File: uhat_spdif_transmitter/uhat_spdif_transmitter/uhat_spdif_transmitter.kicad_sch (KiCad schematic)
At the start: 75 parts, among them J1 GPIO_CONNECTOR, Q1 SS8050, SW1 SW_Push, U1 PLT131/T8, U10 USBLC6-2SC6, U2 LR8103A-T12, U4 W25Q32JVSSIQ, U5 24LC256T-I/SN, U6 PLT131/T8, U8 ICE40UP5K-SG48I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

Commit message: layout
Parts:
- removed SW1: SW_Push, Button_Switch_SMD:SW_SPST_EVQQ2, symbol Switch:SW_Push
- added J2: Conn_02x03_Odd_Even, Connector_PinHeader_2.54mm:PinHeader_2x03_P2.54mm_Vertical_SMD, symbol Connector_Generic:Conn_02x03_Odd_Even
- added J3: Conn_01x03_Pin, Connector_PinHeader_2.54mm:PinHeader_1x03_P2.54mm_Vertical_SMD_Pin1Left, symbol Connector:Conn_01x03_Pin
- added SW1: SPEH110100, Locrius_KiCad:SW-SMD_L6.0-W6.0-LS6.6, symbol Locrius_KiCad:SPEH110100
- R3, R4: value 27R -> 68R
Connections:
- net QSPI_SCLK is gone; now on net SPI_SCK: U8.15 (IOB_34a_SPI_SCK)
- net QSPI_SD0 is gone; now on net SPI_MOSI: U8.14 (IOB_32a_SPI_SO)
- net QSPI_SD1 is gone; now on net SPI_MISO: U8.17 (IOB_33b_SPI_SI)
- net QSPI_SS is gone; now on net SPI_SS: U8.16 (IOB_35b_SPI_SS)
- net GND: now also J2.5 (Pin_5), J2.6 (Pin_6), J3.3 (Pin_3), SW1.1
- net PCM_BCLK: now also J2.2 (Pin_2); no longer R13.2
- net PCM_DOUT: now also J2.1 (Pin_1); no longer R14.2
- net PCM_FCLK: now also J3.1 (Pin_1); no longer R12.2
- net USER_SW: now also SW1.2
- net DM renamed DN
- net QSPI_SD2: no longer names the net of U8.10 (IOB_18a)
- net QSPI_SD3: no longer names the net of U8.20 (IOB_25b_G3)
- new net FPGA_BCLK: J2.4 (Pin_4), R13.2
- new net FPGA_DOUT: J2.3 (Pin_3), R14.2
- new net FPGA_FCLK: J3.2 (Pin_2), R12.2
- no-connect marks 25 -> 41
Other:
- note added: "APX Header"

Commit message: Finish routing
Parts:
- removed D7: C2290, LED_SMD:LED_0805_2012Metric, symbol Device:LED
- removed LED1: TC5050RGBF08-3CJH-AF53A, Locrius_KiCad:LED-SMD_6P-L5.0-W5.0-TL_TC5050RGBF08, symbol Locrius_KiCad:TC5050RGBF08-3CJH-AF53A
- removed Q1: SS8050, Package_TO_SOT_SMD:SOT-23, symbol Transistor_BJT:SS8050
- removed R26: 2k2, Resistor_SMD:R_0603_1608Metric_Pad0.98x0.95mm_HandSolder, symbol Device:R
- removed SW1: SPEH110100, Locrius_KiCad:SW-SMD_L6.0-W6.0-LS6.6, symbol Locrius_KiCad:SPEH110100
- removed U1, U6: PLT131/T8, Locrius_KiCad:OPTO-TH_PLT131-T8, symbol Locrius_KiCad:PLT131_T8
- added J4: Conn_02x03_Odd_Even, Connector_PinHeader_2.54mm:PinHeader_2x03_P2.54mm_Vertical, symbol Connector_Generic:Conn_02x03_Odd_Even
- added LED2: MHS110RGBCT, Locrius_KiCad:LED-ARRAY-SMD_MHS110RGBCT, symbol Locrius_KiCad:MHS110RGBCT
- added SW2: SKRTLAE010, Locrius_KiCad:KEY-SMD_SKRTLAE010, symbol Locrius_KiCad:SKRTLAE010
- added U1, U6: PLR237/T10BK, Locrius_KiCad:OPTO-TH_PLR237-T10BK, symbol Locrius_KiCad:PLR237_T10BK
- J2: footprint Connector_PinHeader_2.54mm:PinHeader_2x03_P2.54mm_Vertical_SMD -> Connector_PinHeader_2.54mm:PinHeader_2x03_P2.54mm_Vertical
- J3: footprint Connector_PinHeader_2.54mm:PinHeader_1x03_P2.54mm_Vertical_SMD_Pin1Left -> Connector_PinHeader_2.54mm:PinHeader_1x03_P2.54mm_Vertical
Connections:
- net +3V3: now also LED2.2 (+)
- net GND: now also J4.1 (Pin_1), J4.3 (Pin_3), J4.5 (Pin_5), SW2.1, SW2.3, SW2.4, SW2.5, U1.2 (GND), U6.2 (GND)
- net OPT1: now also U1.3 (VOUT)
- net OPT2: now also U6.3 (VOUT)
- net USER_SW: now also SW2.2
- net at C13.1, FB2.2: now also U6.1 (VCC)
- net at R18.2: now also LED2.1 (-)
- net at C12.1, FB1.2: now also U1.1 (VCC)
- net at R19.2: now also LED2.3 (-)
- net at R20.2: now also LED2.4 (-)
- net at U8.10 (IOB_18a): now also J4.4 (Pin_4)
- net at U8.11 (IOB_20a): now also J4.6 (Pin_6)
- net at U8.9 (IOB_16a): now also J4.2 (Pin_2)
- net USER_LED: no longer names the net of U8.19 (IOB_29b)
- no-connect marks 41 -> 43
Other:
- moved on the sheet: R18, R19, R20

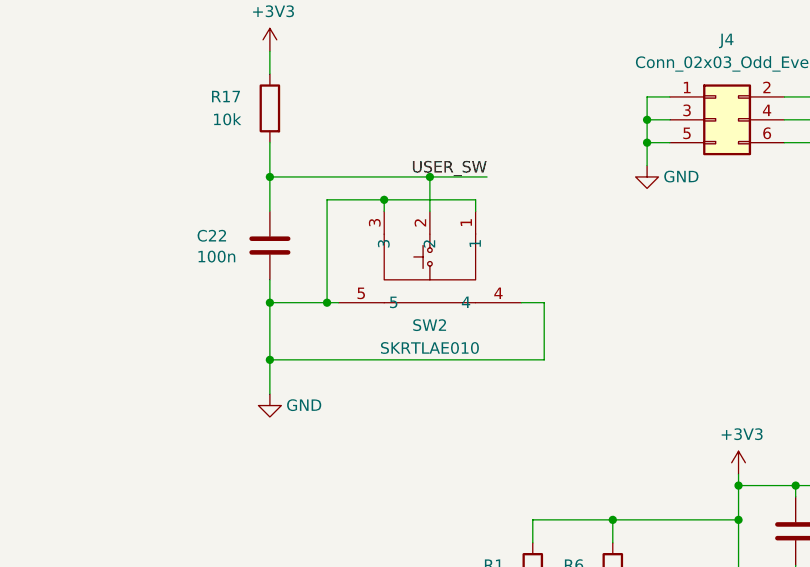
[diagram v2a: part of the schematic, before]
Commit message: Change push button, add barcode location
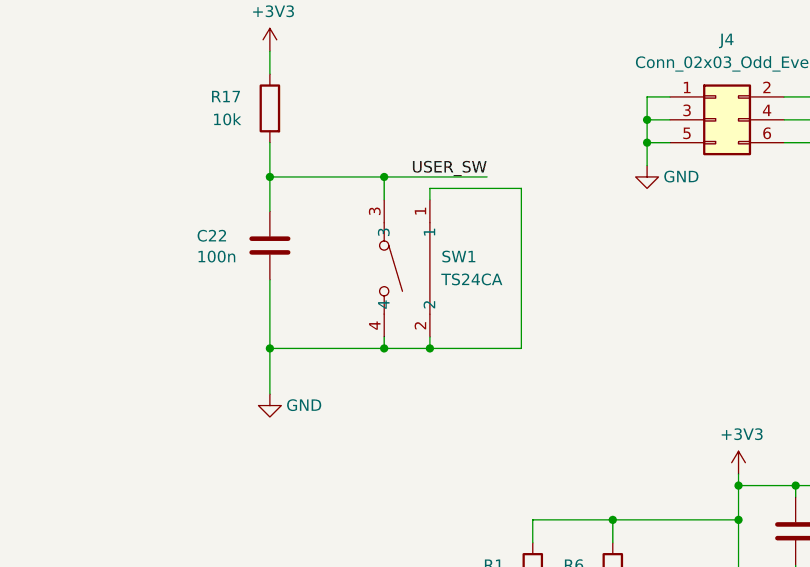
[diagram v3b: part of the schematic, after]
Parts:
- removed SW2: SKRTLAE010, Locrius_KiCad:KEY-SMD_SKRTLAE010, symbol Locrius_KiCad:SKRTLAE010
- added SW1: TS24CA, Locrius_KiCad:SW-SMD_TS24CA, symbol Locrius_KiCad:TS24CA
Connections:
- net GND: now also SW1.1, SW1.2, SW1.4
- net USER_SW: now also SW1.3

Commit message: Change Optical Connector + other stuff
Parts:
- U1, U6: symbol Locrius_KiCad:PLR237_T10BK -> Locrius_KiCad:PLT237_T10WH
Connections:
- net GND: now also U1.3 (GND), U6.3 (GND); no longer U1.2 (GND), U6.2 (GND)
- net OPT1: now also U1.1 (VOUT); no longer U1.3 (VOUT)
- net OPT2: now also U6.1 (VOUT); no longer U6.3 (VOUT)
- net at C12.1, FB1.2: now also U1.2 (VCC); no longer U1.1 (VCC)
- net at C13.1, FB2.2: now also U6.2 (VCC); no longer U6.1 (VCC)
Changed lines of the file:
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@@
 	)
 	(symbol
-		(lib_id "Locrius_KiCad:PLR237_T10BK")
+		(lib_id "Locrius_KiCad:PLT237_T10WH")
 		(at 384.81 86.36 0)
 		(unit 1)
@@
 	)
 	(symbol
-		(lib_id "Locrius_KiCad:PLR237_T10BK")
+		(lib_id "Locrius_KiCad:PLT237_T10WH")
 		(at 384.81 113.03 0)
 		(unit 1)
